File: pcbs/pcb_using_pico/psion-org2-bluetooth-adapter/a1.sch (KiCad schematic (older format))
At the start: 10 parts, among them J2 Conn_01x03_Female, M1 P-CHANNEL-MOSFET, U4 ESP32-WROOM-32

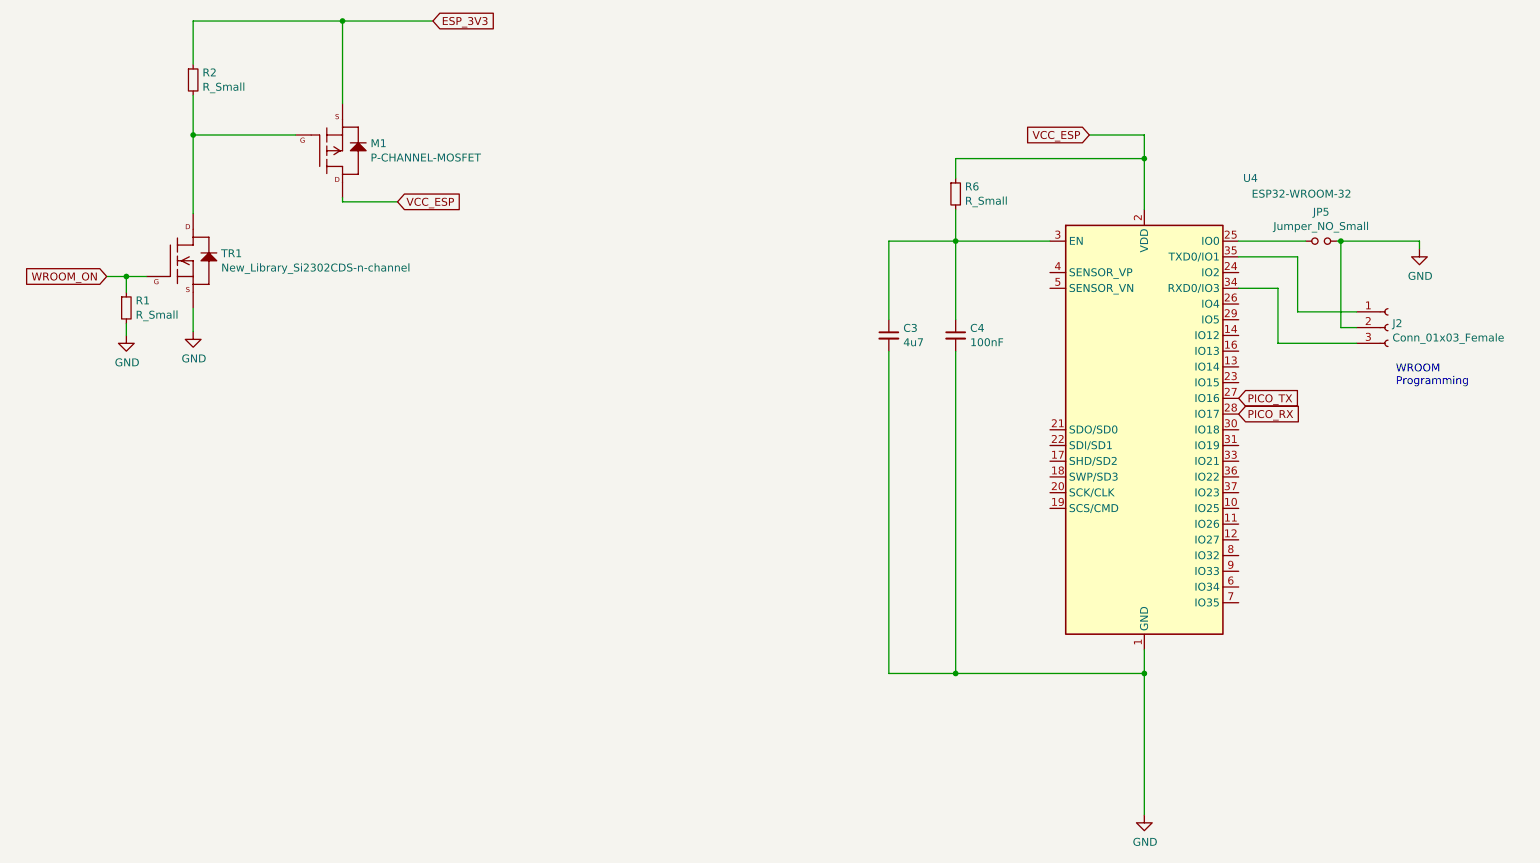
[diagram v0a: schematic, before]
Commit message: Merged erroneous changes to V1.0 archive started
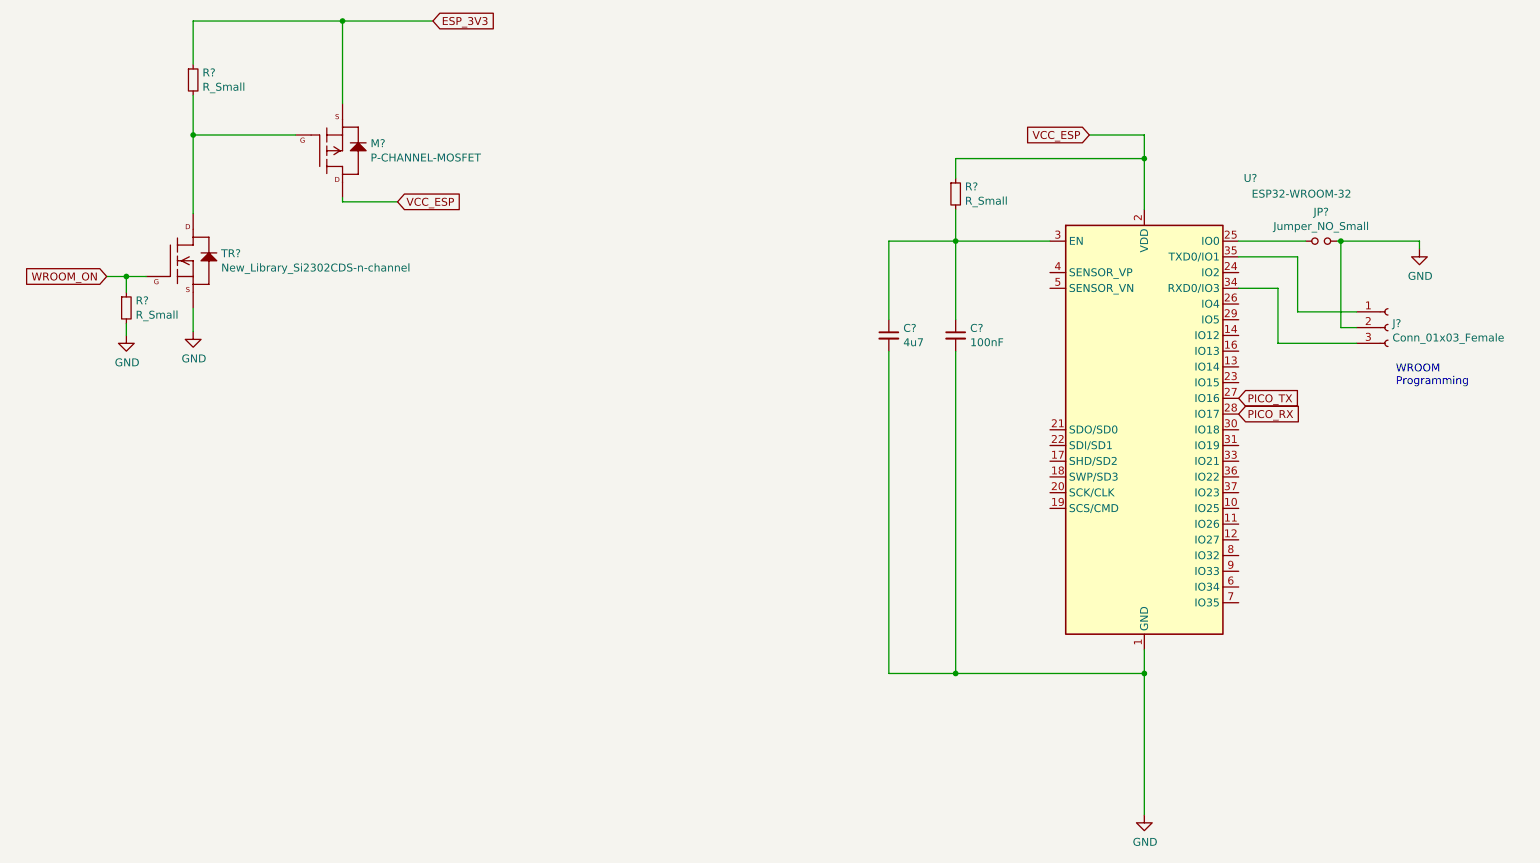
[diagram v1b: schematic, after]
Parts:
- removed M1: P-CHANNEL-MOSFET, Package_TO_SOT_SMD:SOT-23, symbol GeekAmmo:P-CHANNEL-MOSFET
- removed R2: R_Small, Resistor_SMD:R_0805_2012Metric, symbol Device:R_Small
- removed TR1: New_Library_Si2302CDS-n-channel, Package_TO_SOT_SMD:SOT-23, symbol cq1re1-cache:New_Library_Si2302CDS-n-channel
- added M?: P-CHANNEL-MOSFET, Package_TO_SOT_SMD:SOT-23, symbol GeekAmmo:P-CHANNEL-MOSFET
- added R?: R_Small, Resistor_SMD:R_0805_2012Metric, symbol Device:R_Small
- added TR?: New_Library_Si2302CDS-n-channel, Package_TO_SOT_SMD:SOT-23, symbol cq1re1-cache:New_Library_Si2302CDS-n-channel
- renumbered R1 to R?
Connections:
- net ESP_3V3: now also M?.2 (S), R?.1
- net GND: now also TR?.2 (S)
- net VCC_ESP: now also M?.3 (D)
- net WROOM_ON: now also TR?.1 (G)
- new net: M?.1 (G), R?.2, TR?.3 (D)
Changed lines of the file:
@@
 $Descr A4 11693 8268
 encoding utf-8
-Sheet 2 3
+Sheet 4 6
 Title ""
 Date ""
@@
 $Comp
 L RF_Module:ESP32-WROOM-32 U?
-U 1 1 620E66A9
+U 1 1 62097983
 P 8000 3350
-AR Path="/61D041C0/61D04600/620E66A9" Ref="U?"  Part="1"
-AR Path="/61D041C0/620E66A9" Ref="U4"  Part="1"
-F 0 "U4" H 8675 4950 50  0000 C CNN
+AR Path="/61D041C0/61D04600/62097983" Ref="U?"  Part="1"
+AR Path="/61D041C0/62097983" Ref="U4"  Part="1"
+AR Path="/61D0535C/620972E4/62097983" Ref="U?"  Part="1"
+F 0 "U?" H 8675 4950 50  0000 C CNN
 F 1 "ESP32-WROOM-32" H 9000 4850 50  0000 C CNN
 F 2 "RF_Module:ESP32-WROOM-32" H 8000 1850 50  0001 C CNN
@@
 $Comp
 L Device:R_Small R?
-U 1 1 61D1E6BC
+U 1 1 62097984
 P 6800 1850
-AR Path="/61D041C0/61D04600/61D1E6BC" Ref="R?"  Part="1"
-AR Path="/61D041C0/61D1E6BC" Ref="R6"  Part="1"
-F 0 "R6" H 6859 1896 50  0000 L CNN
+AR Path="/61D041C0/61D04600/62097984" Ref="R?"  Part="1"
+AR Path="/61D041C0/62097984" Ref="R6"  Part="1"
+AR Path="/61D0535C/620972E4/62097984" Ref="R?"  Part="1"
+F 0 "R?" H 6859 1896 50  0000 L CNN
 F 1 "R_Small" H 6859 1805 50  0000 L CNN
 F 2 "Resistor_SMD:R_0805_2012Metric" H 6800 1850 50  0001 C CNN
@@
 $Comp
 L Device:C_Small C?
-U 1 1 61D1E6C8
+U 1 1 62097985
 P 6800 2750
-AR Path="/61D041C0/61D04600/61D1E6C8" Ref="C?"  Part="1"
-AR Path="/61D041C0/61D1E6C8" Ref="C4"  Part="1"
-F 0 "C4" H 6892 2796 50  0000 L CNN
+AR Path="/61D041C0/61D04600/62097985" Ref="C?"  Part="1"
+AR Path="/61D041C0/62097985" Ref="C4"  Part="1"
+AR Path="/61D0535C/620972E4/62097985" Ref="C?"  Part="1"
+F 0 "C?" H 6892 2796 50  0000 L CNN
 F 1 "100nF" H 6892 2705 50  0000 L CNN
 F 2 "Capacitor_SMD:C_0805_2012Metric" H 6800 2750 50  0001 C CNN
@@
 $Comp
 L power:GND #PWR?
-U 1 1 620E66AC
+U 1 1 62097986
 P 8000 5800
-AR Path="/61D041C0/61D04600/620E66AC" Ref="#PWR?"  Part="1"
-AR Path="/61D041C0/620E66AC" Ref="#PWR0116"  Part="1"
-F 0 "#PWR0116" H 8000 5550 50  0001 C CNN
+AR Path="/61D041C0/61D04600/62097986" Ref="#PWR?"  Part="1"
+AR Path="/61D041C0/62097986" Ref="#PWR0116"  Part="1"
+AR Path="/61D0535C/620972E4/62097986" Ref="#PWR?"  Part="1"
+F 0 "#PWR?" H 8000 5550 50  0001 C CNN
 F 1 "GND" H 8005 5627 50  0000 C CNN
 F 2 "" H 8000 5800 50  0001 C CNN
@@
 $Comp
 L Device:Jumper_NO_Small JP?
-U 1 1 61D1E6DE
+U 1 1 62097987
 P 9125 2150
-AR Path="/61D041C0/61D04600/61D1E6DE" Ref="JP?"  Part="1"
-AR Path="/61D041C0/61D1E6DE" Ref="JP5"  Part="1"
-F 0 "JP5" H 9125 2335 50  0000 C CNN
+AR Path="/61D041C0/61D04600/62097987" Ref="JP?"  Part="1"
+AR Path="/61D041C0/62097987" Ref="JP5"  Part="1"
+AR Path="/61D0535C/620972E4/62097987" Ref="JP?"  Part="1"
+F 0 "JP?" H 9125 2335 50  0000 C CNN
 F 1 "Jumper_NO_Small" H 9125 2244 50  0000 C CNN
 F 2 "Jumper:SolderJumper-2_P1.3mm_Open_RoundedPad1.0x1.5mm" H 9125 2150 50  0001 C CNN
@@
 AR Path="/61D041C0/61D04600/61D1E6E4" Ref="#PWR?"  Part="1"
 AR Path="/61D041C0/61D1E6E4" Ref="#PWR0117"  Part="1"
-F 0 "#PWR0117" H 9750 1950 50  0001 C CNN
+AR Path="/61D0535C/620972E4/61D1E6E4" Ref="#PWR?"  Part="1"
+F 0 "#PWR?" H 9750 1950 50  0001 C CNN
 F 1 "GND" H 9755 2027 50  0000 C CNN
 F 2 "" H 9750 2200 50  0001 C CNN
@@
 $Comp
 L Connector:Conn_01x03_Female J?
-U 1 1 61D1E6ED
+U 1 1 62097989
 P 9550 2700
-AR Path="/61D041C0/61D04600/61D1E6ED" Ref="J?"  Part="1"
-AR Path="/61D041C0/61D1E6ED" Ref="J2"  Part="1"
-F 0 "J2" H 9578 2726 50  0000 L CNN
+AR Path="/61D041C0/61D04600/62097989" Ref="J?"  Part="1"
+AR Path="/61D041C0/62097989" Ref="J2"  Part="1"
+AR Path="/61D0535C/620972E4/62097989" Ref="J?"  Part="1"
+F 0 "J?" H 9578 2726 50  0000 L CNN
 F 1 "Conn_01x03_Female" H 9578 2635 50  0000 L CNN
 F 2 "Connector_PinHeader_2.54mm:PinHeader_1x03_P2.54mm_Vertical_SMD_Pin1Left" H 9550 2700 50  0001 C CNN
@@
 AR Path="/61D041C0/61D04600/61D1E6FC" Ref="C?"  Part="1"
 AR Path="/61D041C0/61D1E6FC" Ref="C3"  Part="1"
-F 0 "C3" H 6467 2796 50  0000 L CNN
+AR Path="/61D0535C/620972E4/61D1E6FC" Ref="C?"  Part="1"
+F 0 "C?" H 6467 2796 50  0000 L CNN
 F 1 "4u7" H 6467 2705 50  0000 L CNN
 F 2 "Capacitor_SMD:C_1206_3216Metric_Pad1.42x1.75mm_HandSolder" H 6375 2750 50  0001 C CNN
@@
 WROOM\nProgramming
 $Comp
-L Device:R_Small R2
-U 1 1 620E66BF
+L Device:R_Small R?
+U 1 1 61D4E017
 P 1950 1125
-F 0 "R2" H 2009 1171 50  0000 L CNN
+F 0 "R?" H 2009 1171 50  0000 L CNN
 F 1 "R_Small" H 2009 1080 50  0000 L CNN
 F 2 "Resistor_SMD:R_0805_2012Metric" H 1950 1125 50  0001 C CNN
@@
 $EndComp
 $Comp
-L power:GND #PWR0118
+L power:GND #PWR?
 U 1 1 61D4EA71
 P 1950 2725
-F 0 "#PWR0118" H 1950 2475 50  0001 C CNN
+F 0 "#PWR?" H 1950 2475 50  0001 C CNN
 F 1 "GND" H 1955 2552 50  0000 C CNN
 F 2 "" H 1950 2725 50  0001 C CNN
@@
 	1650 2375 1525 2375
 $Comp
-L Device:R_Small R1
+L Device:R_Small R?
 U 1 1 61D504F1
 P 1525 2575
-F 0 "R1" H 1584 2621 50  0000 L CNN
+F 0 "R?" H 1584 2621 50  0000 L CNN
 F 1 "R_Small" H 1584 2530 50  0000 L CNN
 F 2 "Resistor_SMD:R_0805_2012Metric" H 1525 2575 50  0001 C CNN
@@
 $EndComp
 $Comp
-L power:GND #PWR0119
-U 1 1 620E66C2
+L power:GND #PWR?
+U 1 1 6209798E
 P 1525 2750
-F 0 "#PWR0119" H 1525 2500 50  0001 C CNN
+F 0 "#PWR?" H 1525 2500 50  0001 C CNN
 F 1 "GND" H 1530 2577 50  0000 C CNN
 F 2 "" H 1525 2750 50  0001 C CNN
@@
 	2900 1900 3250 1900
 $Comp
-L cq1re1-cache:New_Library_Si2302CDS-n-channel TR1
-U 1 1 620E6686
+L cq1re1-cache:New_Library_Si2302CDS-n-channel TR?
+U 1 1 62097981
 P 1850 2275
-F 0 "TR1" H 2128 2321 50  0000 L CNN
+F 0 "TR?" H 2128 2321 50  0000 L CNN
 F 1 "New_Library_Si2302CDS-n-channel" H 2128 2230 50  0000 L CNN
 F 2 "Package_TO_SOT_SMD:SOT-23" H 1880 2425 20  0001 C CNN
@@
 $EndComp
 $Comp
-L GeekAmmo:P-CHANNEL-MOSFET M1
-U 1 1 620E6687
+L GeekAmmo:P-CHANNEL-MOSFET M?
+U 1 1 62097982
 P 2800 1575
-F 0 "M1" H 3078 1621 50  0000 L CNN
+F 0 "M?" H 3078 1621 50  0000 L CNN
 F 1 "P-CHANNEL-MOSFET" H 3078 1530 50  0000 L CNN
 F 2 "Package_TO_SOT_SMD:SOT-23" H 2830 1725 20  0001 C CNN
